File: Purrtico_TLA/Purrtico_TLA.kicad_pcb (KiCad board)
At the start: 2 copper layers, 100 x 50 mm, 65 parts, among them J1 XLR3, J2 Conn_01x03, J3 Conn_01x02, J4 XLR3, J5 Conn_01x02, U1 OPA1679, U2 OPA1679

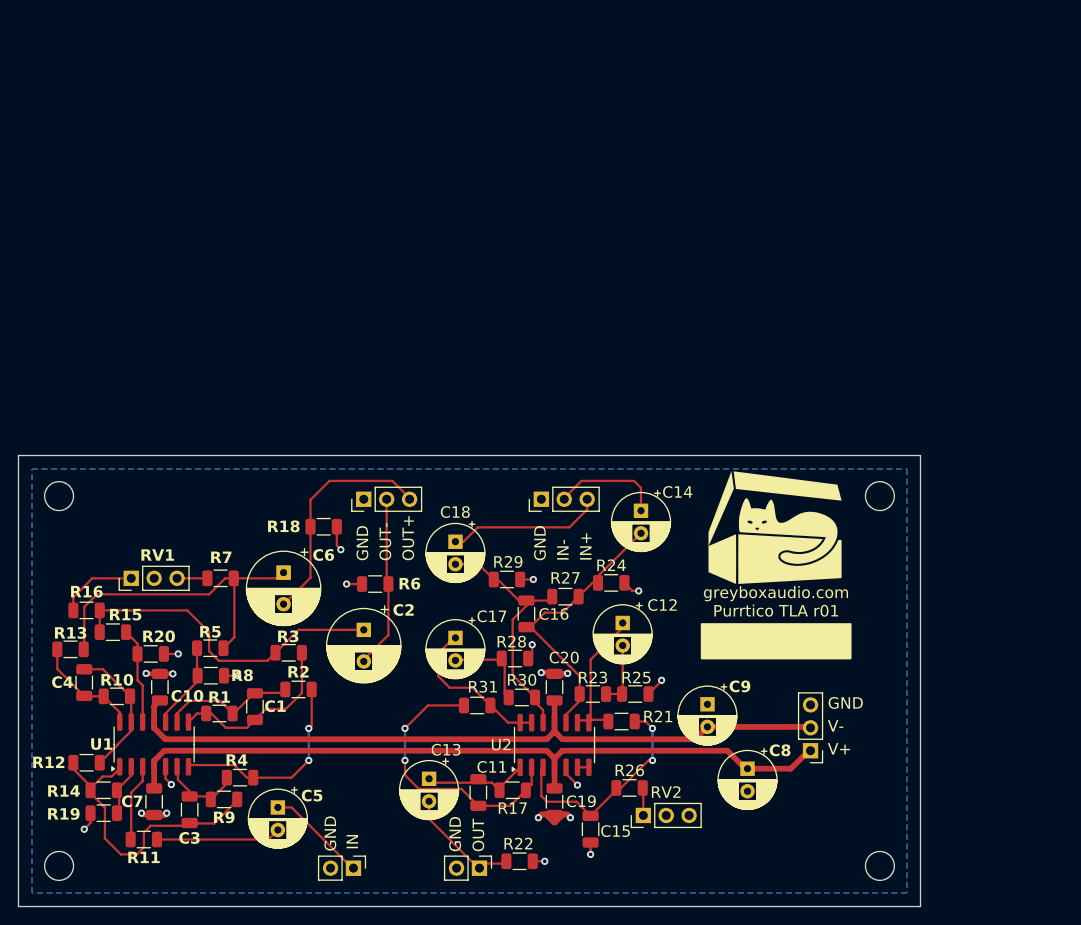
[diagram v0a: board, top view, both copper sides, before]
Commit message: 2k2 & mounting
made R7 & R16 equal value, added copper mounting holes
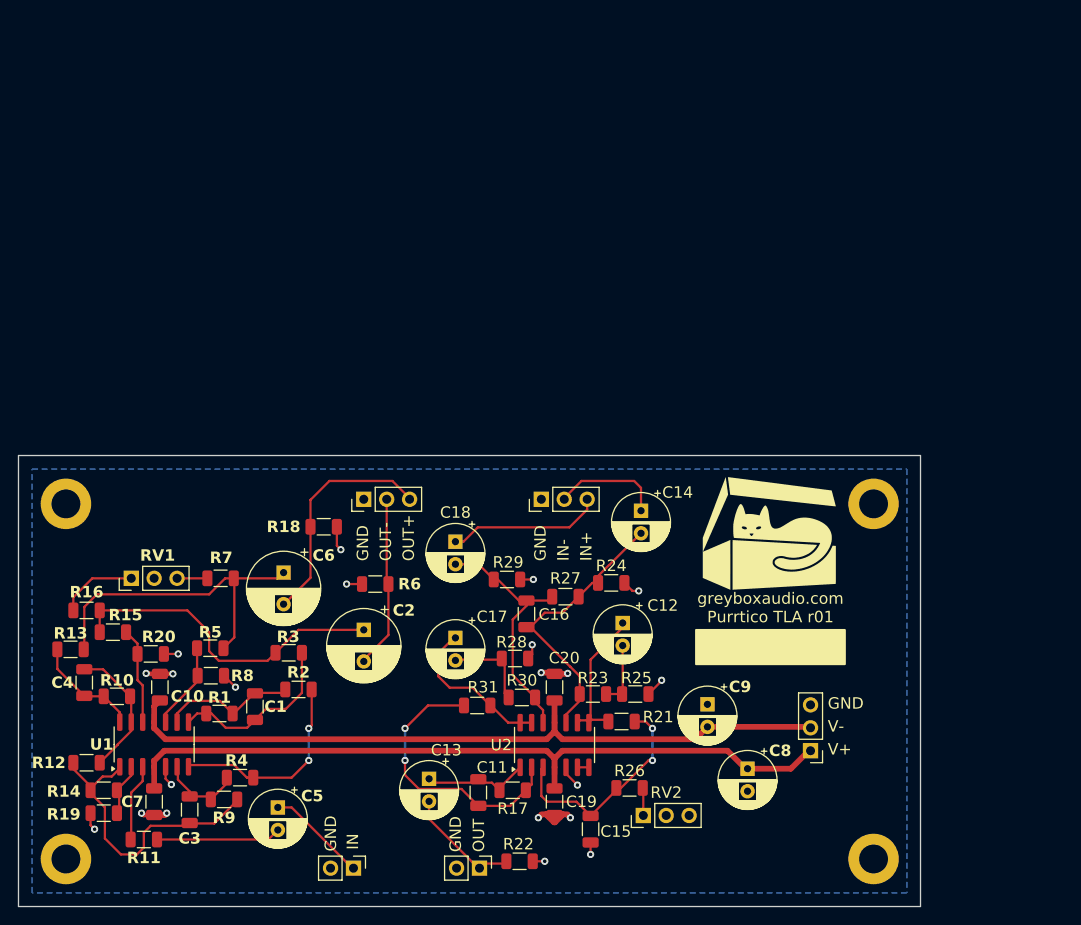
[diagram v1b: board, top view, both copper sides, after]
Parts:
- H1, H2, H3, H4: footprint MountingHole:MountingHole_3.2mm_M3_DIN965 -> MountingHole:MountingHole_3.2mm_M3_DIN965_Pad
- R7: value 3k3 -> 2k2
- moved H1 1.15 mm to (48.3, 86.4)
- moved H2 1.11 mm to (137.8, 86.4)
- moved H3 1.08 mm to (48.3, 125.7)
- moved H4 1.04 mm to (137.8, 125.7)
- moved G*** 0.90 mm to (126.4, 89.6)
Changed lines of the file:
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@@
 		)
 	)
-	(footprint "MountingHole:MountingHole_3.2mm_M3_DIN965"
+	(footprint "MountingHole:MountingHole_3.2mm_M3_DIN965_Pad"
 		(layer "F.Cu")
-		(at 47.5 85.5)
-		(descr "Mounting Hole 3.2mm, no annular, M3, DIN965")
-		(tags "mounting hole 3.2mm no annular m3 din965")
+		(at 48.26 86.36)
+		(descr "Mounting Hole 3.2mm, M3, DIN965")
+		(tags "mounting hole 3.2mm m3 din965")
 		(property "Reference" "H1"
 			(at 0 -3.8 0)
@@
 			)
 		)
-		(property "Footprint" "MountingHole:MountingHole_3.2mm_M3_DIN965"
+		(property "Footprint" "MountingHole:MountingHole_3.2mm_M3_DIN965_Pad"
 			(at 0 0 0)
 			(unlocked yes)
@@
 			)
 		)
-		(property "Description" "Mounting Hole without connection"
+		(property "Description" "Mounting Hole with connection"
 			(at 0 0 0)
 			(unlocked yes)
@@
 			)
 		)
-		(property ki_fp_filters "MountingHole*")
+		(property ki_fp_filters "MountingHole*Pad*")
 		(sheetname "Root")
 		(sheetfile "Purrtico_TLA.kicad_sch")
@@
 			)
 		)
-		(pad "" np_thru_hole circle
+		(pad "1" thru_hole circle
 			(at 0 0)
-			(size 3.2 3.2)
+			(size 5.6 5.6)
 			(drill 3.2)
 			(layers "*.Cu" "*.Mask")
+			(remove_unused_layers no)
+			(net 15 "GND")
+			(pinfunction "1")
+			(pintype "input")
 		)
 	)
@@
 		)
 	)
-	(footprint "MountingHole:MountingHole_3.2mm_M3_DIN965"
+	(footprint "MountingHole:MountingHole_3.2mm_M3_DIN965_Pad"
 		(layer "F.Cu")
-		(at 138.5 85.5)
-		(descr "Mounting Hole 3.2mm, no annular, M3, DIN965")
-		(tags "mounting hole 3.2mm no annular m3 din965")
+		(at 137.795 86.36)
+		(descr "Mounting Hole 3.2mm, M3, DIN965")
+		(tags "mounting hole 3.2mm m3 din965")
 		(property "Reference" "H2"
 			(at 0 -3.8 0)
@@
 			)
 		)
-		(property "Footprint" "MountingHole:MountingHole_3.2mm_M3_DIN965"
+		(property "Footprint" "MountingHole:MountingHole_3.2mm_M3_DIN965_Pad"
 			(at 0 0 0)
 			(unlocked yes)
@@
 			)
 		)
-		(property "Description" "Mounting Hole without connection"
+		(property "Description" "Mounting Hole with connection"
 			(at 0 0 0)
 			(unlocked yes)
@@
 			)
 		)
-		(property ki_fp_filters "MountingHole*")
+		(property ki_fp_filters "MountingHole*Pad*")
 		(sheetname "Root")
 		(sheetfile "Purrtico_TLA.kicad_sch")
@@
 			)
 		)
-		(pad "" np_thru_hole circle
+		(pad "1" thru_hole circle
 			(at 0 0)
-			(size 3.2 3.2)
+			(size 5.6 5.6)
 			(drill 3.2)
 			(layers "*.Cu" "*.Mask")
+			(remove_unused_layers no)
+			(net 15 "GND")
+			(pinfunction "1")
+			(pintype "input")
 		)
 	)
@@
 		)
 	)
-	(footprint "MountingHole:MountingHole_3.2mm_M3_DIN965"
+	(footprint "MountingHole:MountingHole_3.2mm_M3_DIN965_Pad"
 		(layer "F.Cu")
-		(at 47.5 126.5)
-		(descr "Mounting Hole 3.2mm, no annular, M3, DIN965")
-		(tags "mounting hole 3.2mm no annular m3 din965")
+		(at 48.26 125.73)
+		(descr "Mounting Hole 3.2mm, M3, DIN965")
+		(tags "mounting hole 3.2mm m3 din965")
 		(property "Reference" "H3"
 			(at 0 -3.8 0)
@@
 			)
 		)
-		(property "Footprint" "MountingHole:MountingHole_3.2mm_M3_DIN965"
+		(property "Footprint" "MountingHole:MountingHole_3.2mm_M3_DIN965_Pad"
 			(at 0 0 0)
 			(unlocked yes)
@@
 			)
 		)
-		(property "Description" "Mounting Hole without connection"
+		(property "Description" "Mounting Hole with connection"
 			(at 0 0 0)
 			(unlocked yes)
@@
 			)
 		)
-		(property ki_fp_filters "MountingHole*")
+		(property ki_fp_filters "MountingHole*Pad*")
 		(sheetname "Root")
 		(sheetfile "Purrtico_TLA.kicad_sch")
@@
 			)
 		)
-		(pad "" np_thru_hole circle
+		(pad "1" thru_hole circle
 			(at 0 0)
-			(size 3.2 3.2)
+			(size 5.6 5.6)
 			(drill 3.2)
 			(layers "*.Cu" "*.Mask")
+			(remove_unused_layers no)
+			(net 15 "GND")
+			(pinfunction "1")
+			(pintype "input")
 		)
 	)
@@
 	(footprint "LOGO"
 		(layer "F.Cu")
-		(at 127 89)
+		(at 126.365 89.64)
 		(property "Reference" "G***"
 			(at 0 0 0)
@@
 		)
 	)
-	(footprint "MountingHole:MountingHole_3.2mm_M3_DIN965"
+	(footprint "MountingHole:MountingHole_3.2mm_M3_DIN965_Pad"
 		(layer "F.Cu")
-		(at 138.5 126.5)
-		(descr "Mounting Hole 3.2mm, no annular, M3, DIN965")
-		(tags "mounting hole 3.2mm no annular m3 din965")
+		(at 137.795 125.73)
+		(descr "Mounting Hole 3.2mm, M3, DIN965")
+		(tags "mounting hole 3.2mm m3 din965")
 		(property "Reference" "H4"
 			(at 0 -3.8 0)
@@
 			)
 		)
-		(property "Footprint" "MountingHole:MountingHole_3.2mm_M3_DIN965"
+		(property "Footprint" "MountingHole:MountingHole_3.2mm_M3_DIN965_Pad"
 			(at 0 0 0)
 			(unlocked yes)
@@
 			)
 		)
-		(property "Description" "Mounting Hole without connection"
+		(property "Description" "Mounting Hole with connection"
 			(at 0 0 0)
 			(unlocked yes)
@@
 			)
 		)
-		(property ki_fp_filters "MountingHole*")
+		(property ki_fp_filters "MountingHole*Pad*")
 		(sheetname "Root")
 		(sheetfile "Purrtico_TLA.kicad_sch")
@@
 			)
 		)
-		(pad "" np_thru_hole circle
+		(pad "1" thru_hole circle
 			(at 0 0)
-			(size 3.2 3.2)
+			(size 5.6 5.6)
 			(drill 3.2)
 			(layers "*.Cu" "*.Mask")
+			(remove_unused_layers no)
+			(net 15 "GND")
+			(pinfunction "1")
+			(pintype "input")
 		)
 	)
@@
 			)
 		)
-		(property "Value" "3k3"
+		(property "Value" "2k2"
 			(at 0 1.82 0)
 			(layer "F.Fab")
@@
 	)
 	(gr_rect
-		(start 118.745 99.69)
-		(end 135.255 103.5)
+		(start 118.11 100.33)
+		(end 134.62 104.14)
 		(stroke
 			(width 0.2032)
@@
 	)
 	(gr_text "greyboxaudio.com\nPurrtico TLA r01"
-		(at 127 99 0)
+		(at 126.365 99.64 0)
 		(layer "F.SilkS")
 		(effects
@@
 	)
 	(segment
-		(start 50.9885 121.7315)
-		(end 50.292 122.428)
-		(width 0.254)
-		(layer "F.Cu")
-		(net 15)
-	)
-	(segment
 		(start 56.847 120.855)
 		(end 58.039 120.855)
@@
 	)
 	(segment
-		(start 67.31 105.41)
-		(end 65.786 105.41)
-		(width 0.254)
-		(layer "F.Cu")
-		(net 15)
-	)
-	(segment
 		(start 103.85325 120.777)
 		(end 102.90275 120.777)
@@
 	)
 	(segment
+		(start 67.056 106.68)
+		(end 65.786 105.41)
+		(width 0.254)
+		(layer "F.Cu")
+		(net 15)
+	)
+	(segment
 		(start 114.3 105.918)
 		(end 114.3 105.9835)
@@
 	)
 	(segment
-		(start 50.9885 120.65)
-		(end 50.9885 121.7315)
-		(width 0.254)
-		(layer "F.Cu")
-		(net 15)
-	)
-	(segment
 		(start 103.6975 116.267)
 		(end 104.9675 117.537)
@@
 	)
 	(segment
+		(start 50.9885 121.9815)
+		(end 50.9885 120.65)
+		(width 0.254)
+		(layer "F.Cu")
+		(net 15)
+	)
+	(segment
 		(start 103.837 105.205)
 		(end 102.4275 105.205)
@@
 	)
 	(segment
+		(start 51.435 122.428)
+		(end 50.9885 121.9815)
+		(width 0.254)
+		(layer "F.Cu")
+		(net 15)
+	)
+	(segment
 		(start 100.076 94.742)
 		(end 98.6175 94.742)
@@
 	)
 	(via
-		(at 50.292 122.428)
+		(at 51.435 122.428)
 		(size 0.8)
 		(drill 0.4)
@@
 	)
 	(via
-		(at 67.31 105.41)
+		(at 67.056 106.68)
 		(size 0.8)
 		(drill 0.4)

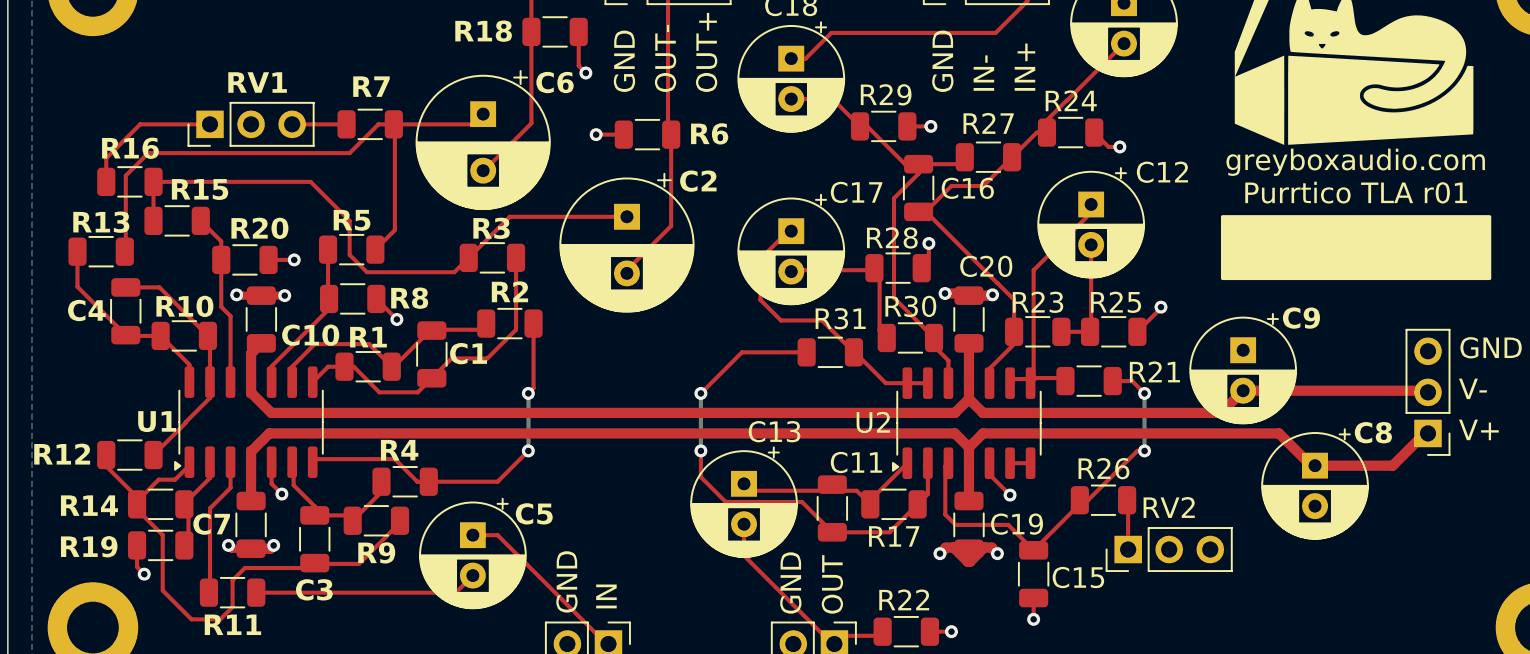
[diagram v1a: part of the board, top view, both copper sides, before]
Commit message: cleaned up tracks
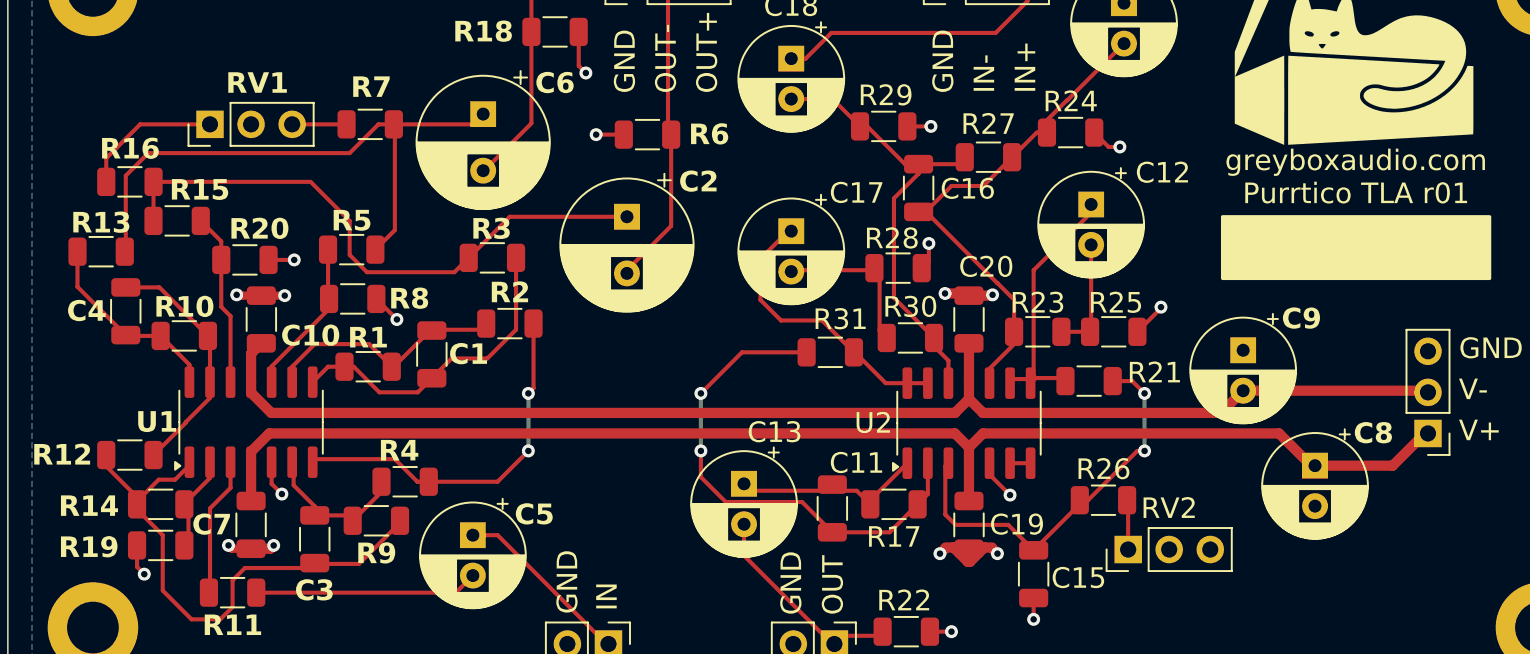
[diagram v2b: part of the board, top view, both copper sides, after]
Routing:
- net Net-(U2A-+): track 26.0 -> 25.0 mm
- net Net-(U2A--): track 32.1 -> 31.1 mm
- net Net-(C3-Pad1): track 35.3 -> 34.5 mm
- net Net-(U2B--): track 1.97 -> 1.27 mm
- net Net-(U1C--): track 15.9 -> 15.2 mm
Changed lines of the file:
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@@
-	)
-	(segment
-		(start 69.215 110.568)
-		(end 69.215 110.314)
-		(width 0.25)
-		(layer "F.Cu")
-		(net 2)
 	)
 	(segment
@@
 	)
 	(segment
-		(start 69.088 110.695)
-		(end 69.215 110.568)
-		(width 0.25)
-		(layer "F.Cu")
-		(net 2)
-	)
-	(segment
 		(start 65.972 111.184)
 		(end 68.345 111.184)
@@
 	)
 	(segment
-		(start 60.522 115.562)
-		(end 60.579 115.505)
-		(width 0.254)
-		(layer "F.Cu")
-		(net 5)
-	)
-	(segment
 		(start 64.3235 119.126)
 		(end 66.1015 117.348)
@@
 	)
 	(segment
-		(start 60.522 115.674115)
-		(end 60.522 115.562)
-		(width 0.254)
-		(layer "F.Cu")
-		(net 5)
-	)
-	(segment
 		(start 61.976 118.794)
 		(end 63.9915 118.794)
@@
 	)
 	(segment
-		(start 54.229 115.505)
-		(end 54.1015 115.3775)
-		(width 0.254)
-		(layer "F.Cu")
-		(net 6)
-	)
-	(segment
 		(start 50.9885 117.6635)
 		(end 49.0835 115.7585)
@@
 	)
 	(segment
-		(start 49.0835 115.062)
-		(end 48.641 115.5045)
-		(width 0.254)
-		(layer "F.Cu")
-		(net 6)
-	)
-	(segment
 		(start 50.9885 118.11)
 		(end 50.9885 117.6635)
@@
 	)
 	(segment
-		(start 69.088 107.491)
-		(end 69.215 107.364)
-		(width 0.254)
-		(layer "F.Cu")
-		(net 8)
-	)
-	(segment
 		(start 66.8675 109.601)
 		(end 69.1045 107.364)
@@
 	)
 	(segment
-		(start 68.58 107.491)
-		(end 69.088 107.491)
-		(width 0.254)
-		(layer "F.Cu")
-		(net 8)
-	)
-	(segment
 		(start 66.7405 109.601)
 		(end 65.3435 108.204)
@@
 		(width 0.635)
 		(layer "F.Cu")
-		(net 14)
-	)
-	(segment
-		(start 130.81 111.187)
-		(end 130.748 111.125)
-		(width 0.635)
-		(layer "B.Cu")
-		(net 14)
-	)
-	(segment
-		(start 119.38 111.085)
-		(end 119.34 111.125)
-		(width 0.635)
-		(layer "B.Cu")
-		(net 14)
-	)
-	(segment
-		(start 119.42 111.125)
-		(end 119.38 111.085)
-		(width 0.635)
-		(layer "B.Cu")
 		(net 14)
 	)
@@
 	)
 	(segment
-		(start 58.039 121.08)
-		(end 58.039 120.855)
-		(width 0.508)
-		(layer "F.Cu")
-		(net 15)
-	)
-	(segment
 		(start 103.85325 120.777)
 		(end 102.90275 120.777)
@@
 	)
 	(segment
-		(start 75.5035 106.934)
-		(end 75.565 106.9955)
-		(width 0.254)
-		(layer "F.Cu")
-		(net 16)
-	)
-	(segment
 		(start 61.9765 115.3775)
 		(end 61.849 115.505)
@@
 	)
 	(segment
-		(start 69.0265 116.5205)
-		(end 69.0265 116.713)
-		(width 0.254)
-		(layer "F.Cu")
-		(net 16)
-	)
-	(segment
 		(start 75.184 111.252)
 		(end 75.5035 110.9325)
@@
 	)
 	(segment
-		(start 56.712 110.498)
-		(end 56.769 110.555)
-		(width 0.254)
-		(layer "F.Cu")
-		(net 22)
-	)
-	(segment
 		(start 56.769 106.4775)
 		(end 56.769 110.555)
@@
 	)
 	(segment
-		(start 88.9 117.221)
-		(end 88.9 117.475)
-		(width 0.254)
-		(layer "F.Cu")
-		(net 23)
-	)
-	(segment
 		(start 95.4875 117.27)
 		(end 93.98 117.27)
@@
 	)
 	(segment
-		(start 93.9925 117.2825)
-		(end 93.98 117.27)
-		(width 0.254)
-		(layer "F.Cu")
-		(net 23)
-	)
-	(segment
 		(start 96.3275 117.857)
 		(end 96.3275 118.11)
@@
 	)
 	(segment
-		(start 104.9675 116.267)
-		(end 104.9675 115.567)
-		(width 0.254)
-		(layer "F.Cu")
-		(net 29)
-	)
-	(segment
 		(start 96.901 103.8245)
 		(end 96.5815 103.505)
@@
 	)
 	(segment
-		(start 100.0145 97.0115)
-		(end 99.949 97.077)
-		(width 0.25)
-		(layer "F.Cu")
-		(net 34)
-	)
-	(segment
 		(start 99.314 97.077)
 		(end 99.314 97.663)
@@
 	)
 	(segment
-		(start 91.44 93.051)
-		(end 91.44 93.091)
-		(width 0.25)
-		(layer "F.Cu")
-		(net 34)
-	)
-	(segment
 		(start 100.2685 107.823)
 		(end 100.2685 108.333)
@@
 	)
 	(segment
-		(start 92.3905 108.712)
-		(end 92.5175 108.712)
-		(width 0.254)
-		(layer "F.Cu")
-		(net 35)
-	)
-	(segment
 		(start 99.2525 118.11)
 		(end 97.5235 119.839)
@@
 	)
 	(segment
-		(start 92.3255 108.647)
-		(end 92.3905 108.712)
-		(width 0.254)
-		(layer "F.Cu")
-		(net 35)
-	)
-	(segment
 		(start 92.108 117.967)
 		(end 93.98 119.839)
@@
 	)
 	(segment
-		(start 92.5175 108.712)
-		(end 92.583 108.7775)
-		(width 0.254)
-		(layer "F.Cu")
-		(net 35)
-	)
-	(segment
 		(start 85.852 116.427)
 		(end 87.392 117.967)
@@
 	)
 	(segment
-		(start 99.8875 115.183264)
-		(end 99.8875 115.567)
-		(width 0.254)
-		(layer "F.Cu")
-		(net 35)
-	)
-	(segment
-		(start 85.852 111.252)
-		(end 85.852 111.252)
-		(width 0.254)
-		(layer "F.Cu")
-		(net 35)
-	)
-	(segment
 		(start 97.5235 119.839)
 		(end 93.98 119.839)
@@
 		(net 35)
 	)
-	(segment
-		(start 99.695 115.7595)
-		(end 99.8875 115.567)
-		(width 0.254)
-		(layer "F.Cu")
-		(net 35)
-	)
 	(via
 		(at 85.852 111.252)
@@
 	)
 	(segment
-		(start 106.426 120.953)
-		(end 106.885 120.953)
-		(width 0.254)
-		(layer "F.Cu")
-		(net 36)
-	)
-	(segment
 		(start 113.284 114.808)
 		(end 112.8375 114.808)
@@
 		(width 0.254)
 		(layer "F.Cu")
-		(net 36)
-	)
-	(segment
-		(start 111.3175 110.302)
-		(end 111.125 110.1095)
-		(width 0.254)
-		(layer "F.Cu")
-		(net 36)
-	)
-	(segment
-		(start 106.6925 120.953)
-		(end 106.426 120.953)
-		(width 0.254)
-		(layer "F.Cu")
